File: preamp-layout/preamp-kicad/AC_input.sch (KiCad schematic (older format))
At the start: 10 parts, among them J2 Screw_Terminal_01x03, J3 Conn_01x02_Female, J4 Conn_01x02_Male, J5 Screw_Terminal_01x03, J6 Conn_01x02_Female, J7 Screw_Terminal_01x03, K1 G5RLU-1A-E

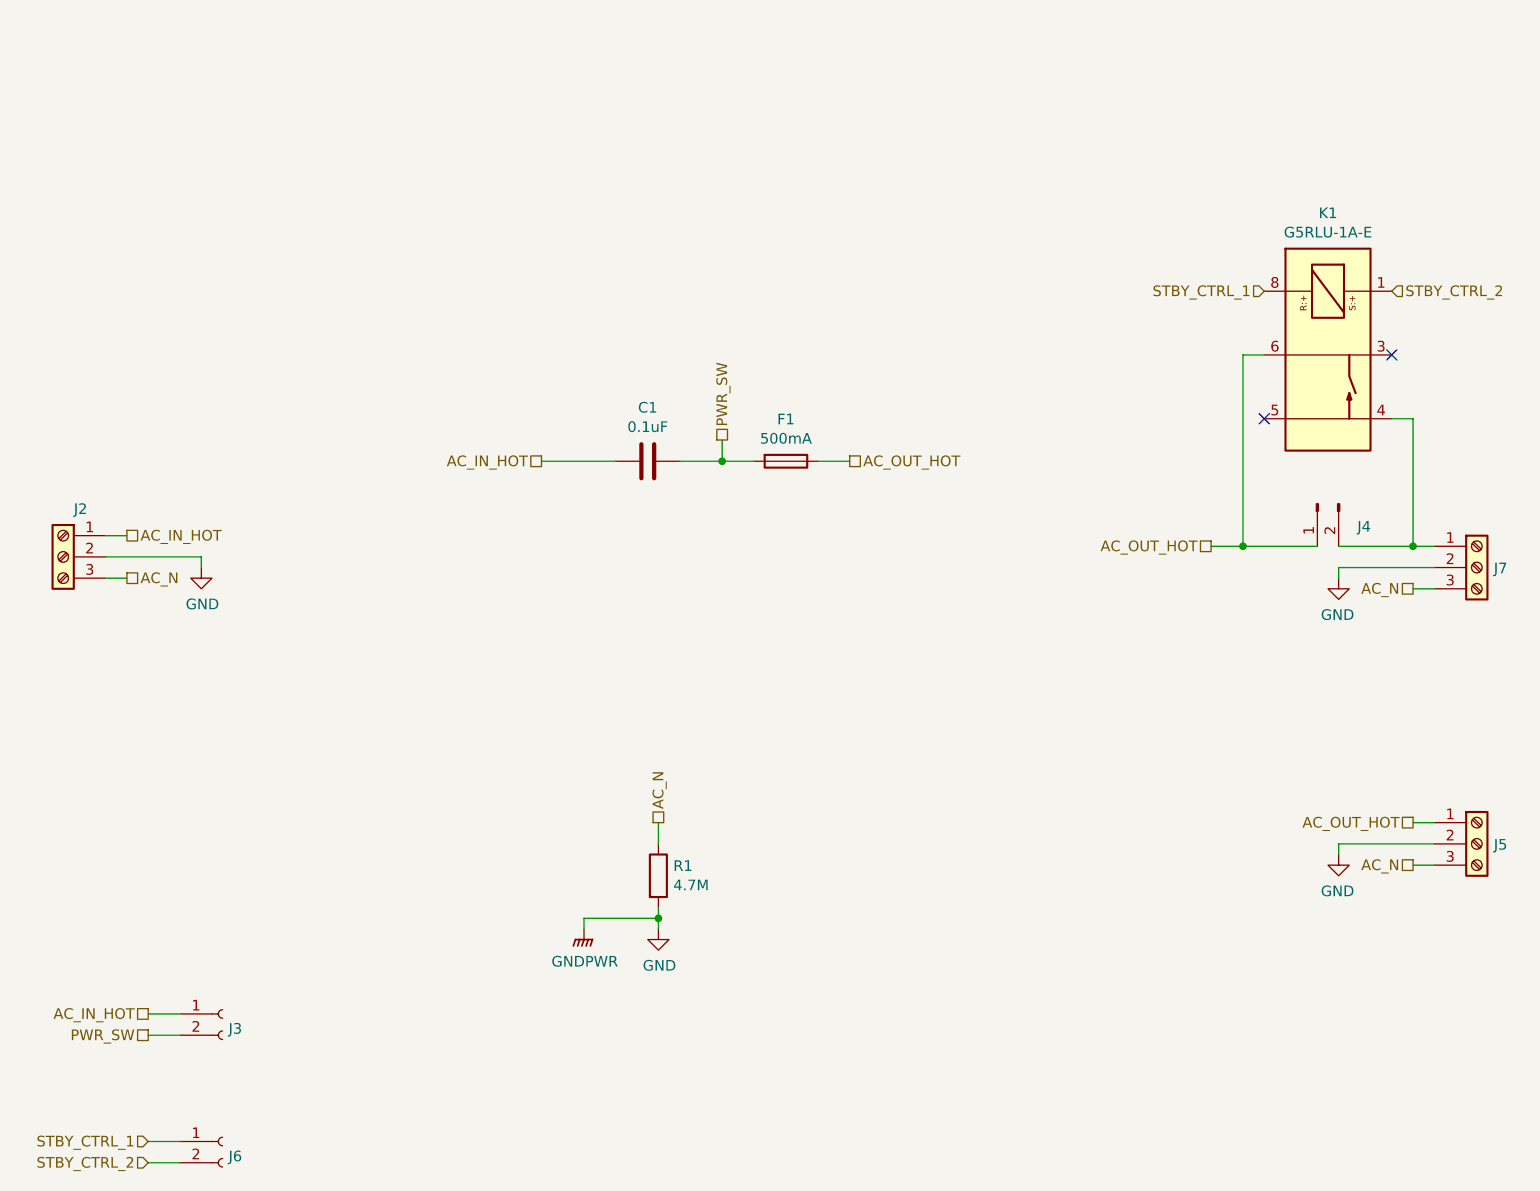
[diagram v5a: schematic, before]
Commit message: RefDes Update
Re-ran refdes assignment, updated BOM accordingly.
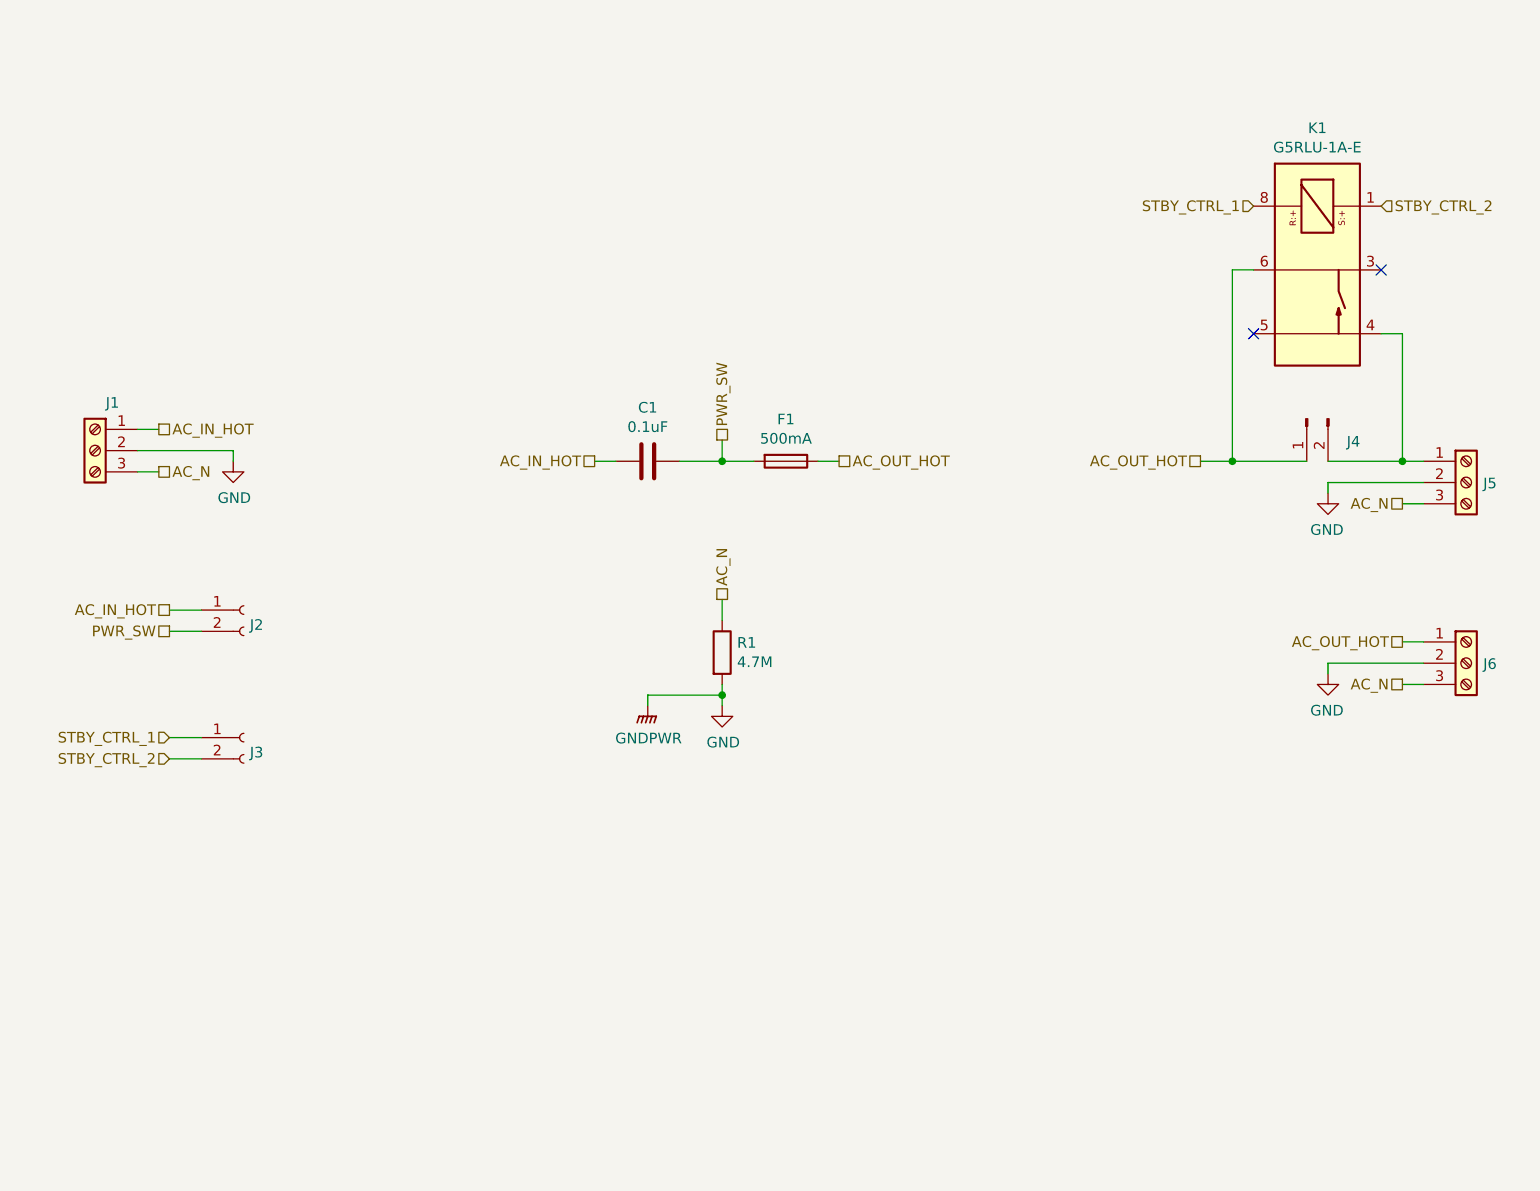
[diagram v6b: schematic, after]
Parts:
- renumbered J2 to J1, J3 to J2, J6 to J3, J7 to J5, J5 to J6
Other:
- moved on the sheet: J1, J2, J3, J4, J5, J6, K1, R1

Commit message: Prelim PCB layout
Work done to lay out PCBs. Saving in anticipation of creating branch with a different input switching topology.
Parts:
- C1: footprint (none) -> Capacitor_SMD:C_1812_4532Metric_Pad1.30x3.40mm_HandSolder
- F1: footprint (none) -> preamp:01110501Z_3AG
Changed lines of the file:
@@
 F 0 "F1" V 5803 3300 50  0000 C CNN
 F 1 "500mA" V 5894 3300 50  0000 C CNN
-F 2 "" V 5930 3300 50  0001 C CNN
+F 2 "preamp:01110501Z_3AG" V 5930 3300 50  0001 C CNN
 F 3 "~" H 6000 3300 50  0001 C CNN
 	1    6000 3300
@@
 F 0 "C1" V 5098 3300 50  0000 C CNN
 F 1 "0.1uF" V 5189 3300 50  0000 C CNN
-F 2 "" H 5388 3150 50  0001 C CNN
+F 2 "Capacitor_SMD:C_1812_4532Metric_Pad1.30x3.40mm_HandSolder" H 5388 3150 50  0001 C CNN
 F 3 "~" H 5350 3300 50  0001 C CNN
 	1    5350 3300

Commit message: Periodic backup
Extensive changes as a result of PCB layout phase.
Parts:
- J4: footprint Connector_JST:JST_EH_B2B-EH-A_1x02_P2.50mm_Vertical -> Connector_PinHeader_2.54mm:PinHeader_1x02_P2.54mm_Vertical
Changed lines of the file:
@@
 F 0 "J4" V 8558 2912 50  0000 R CNN
 F 1 "Conn_01x02_Male" H 8422 2983 50  0001 R CNN
-F 2 "Connector_JST:JST_EH_B2B-EH-A_1x02_P2.50mm_Vertical" H 8450 3100 50  0001 C CNN
+F 2 "Connector_PinHeader_2.54mm:PinHeader_1x02_P2.54mm_Vertical" H 8450 3100 50  0001 C CNN
 F 3 "~" H 8450 3100 50  0001 C CNN
 	1    8450 3100
